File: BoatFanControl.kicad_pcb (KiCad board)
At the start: 2 copper layers, 34 x 34.8 mm, 11 parts, among them J1 Conn_01x04, Q1 IRLIZ44N, SW1 SW_Push, U1 Digispark

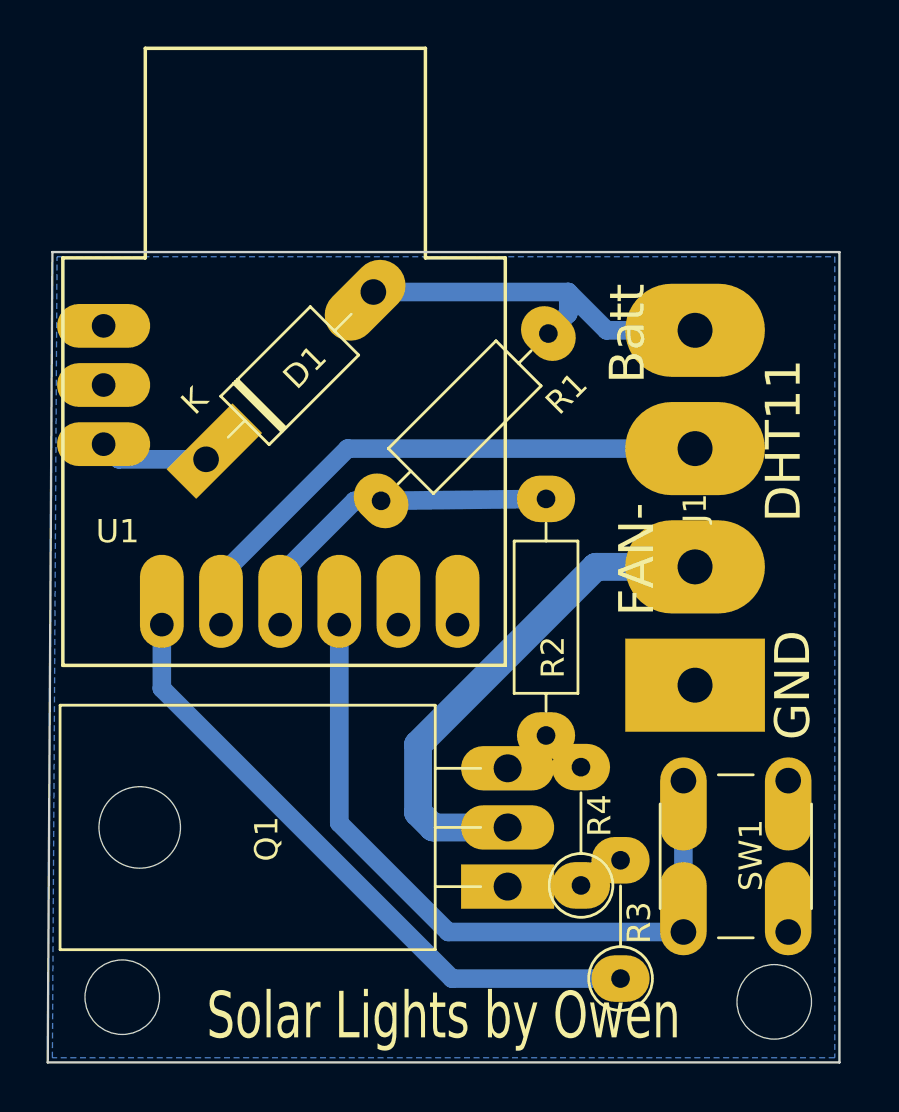
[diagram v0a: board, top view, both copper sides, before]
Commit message: Updated with seperate DHT11 mount
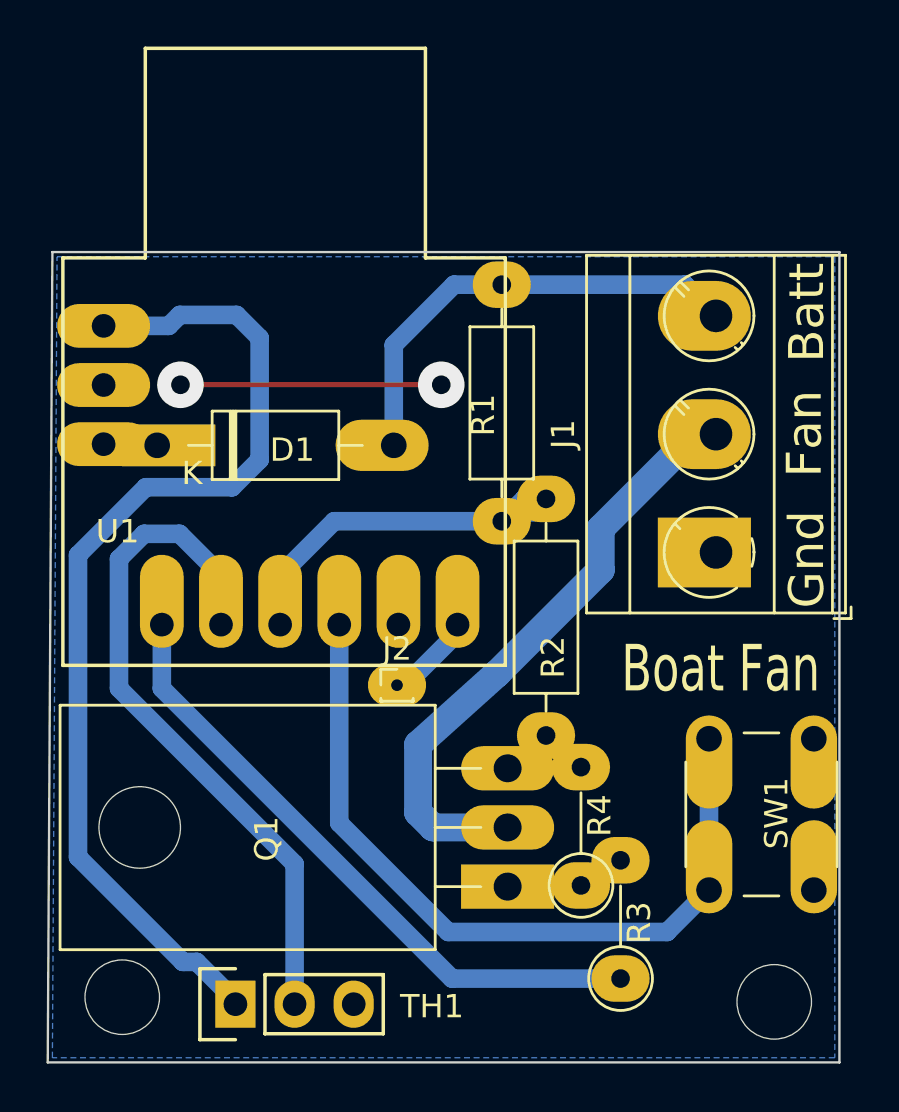
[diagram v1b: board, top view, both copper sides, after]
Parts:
- added J2: Reset, Connector_PinHeader_1.00mm:PinHeader_1x01_P1.00mm_Vertical, F.Cu at (100.0, 83.6)
- added TH1: DHT11, sensors:DHT11_Temperature_Humidity, F.Cu at (95.6, 97.3)
- J1: value Conn_01x04 -> Batt; footprint Connector_Wire:SolderWirePad_1x04_P5.08mm_Drill1.5mm -> TerminalBlock_MetzConnect:TerminalBlock_MetzConnect_Type073_RT02603HBLU_1x03_P5.08mm_Horizontal
- Q1: value IRLIZ44N -> IRLZ14
- R2: value 100R -> 1K
- moved J1 5.77 mm to (113.7, 77.9)
- moved R1 2.90 mm to (104.5, 66.4), turned to 270 degrees
- moved D1 2.18 mm to (89.7, 73.3), turned to 0 degrees
- moved SW1 2.11 mm to (117.9, 85.9)
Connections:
- J1 pad 3: DHT11 -> Vin
- U1 pad 6: (no net) -> Reset
- U1 pad 9: (no net) -> +5V
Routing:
- net +5V: track 0.00 -> 44.5 mm
- net GND: track 2.69 -> 13.9 mm, vias 0 -> 2
- net DHT11: track 24.7 -> 29.9 mm
- net FAN-gnd: track 22.1 -> 26.3 mm
- net Reset: track 0.00 -> 3.88 mm
- net Vin: track 16.6 -> 19.8 mm
- net +BATT: track 4.67 -> 2.32 mm
- net button: track 31.7 -> 33.6 mm
- net Vin-sense: track 14.9 -> 15.7 mm
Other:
- board text added: "Boat Fan"
- board text added: "Fan"
- board text added: "Gnd"
- board text removed: "DHT11"
- board text removed: "FAN-"
- board text removed: "GND"
- board text removed: "Solar Lights by Owen"

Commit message: Case, make PCB square..
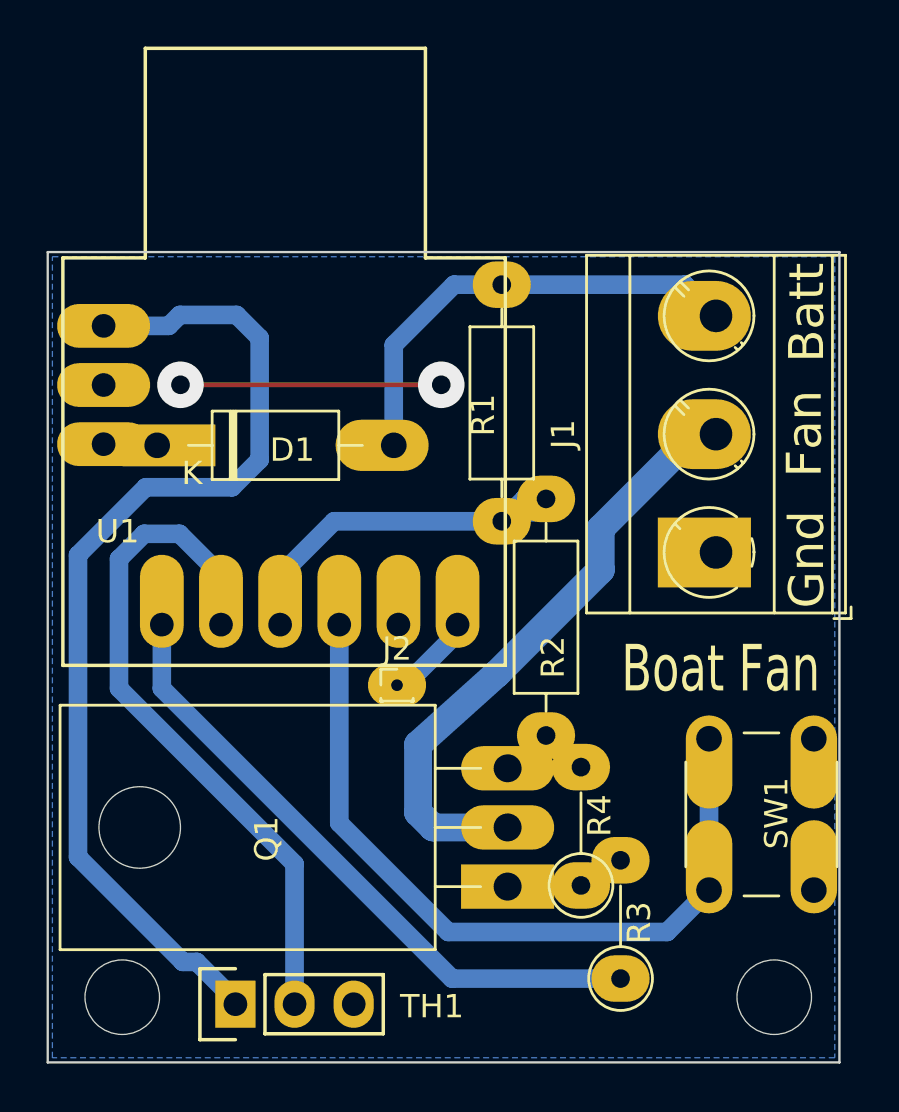
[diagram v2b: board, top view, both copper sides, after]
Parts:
- moved H2 0.20 mm to (116.2, 97.0)
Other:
- outline, holes or cut-outs redrawn
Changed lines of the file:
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@@
     (add_net LED)
     (add_net "Net-(Q1-Pad1)")
-    (add_net "Net-(U1-Pad5)")
     (add_net Reset)
     (add_net Vin)
@@
   )
   (module MountingHole:MountingHole_3.2mm_M3 (layer F.Cu)
-    (at 116.2 97.2)
+    (at 116.2 97)
     (descr "Mounting Hole 3.2mm, no annular, M3")
     (tags "mounting hole 3.2mm no annular m3")
@@
       (effects (font (size 1 1) (thickness 0.15)))
     )
+    (fp_text user %R (at 0.3 0) (layer F.Fab)
+      (effects (font (size 1 1) (thickness 0.15)))
+    )
+    (fp_circle (center 0 0) (end 3.2 0) (layer Cmts.User) (width 0.15))
     (fp_circle (center 0 0) (end 3.45 0) (layer F.CrtYd) (width 0.05))
-    (fp_circle (center 0 0) (end 3.2 0) (layer Cmts.User) (width 0.15))
-    (fp_text user %R (at 0.3 0) (layer F.Fab)
-      (effects (font (size 1 1) (thickness 0.15)))
-    )
     (pad 1 np_thru_hole circle (at 0 0) (size 3.2 3.2) (drill 3.2) (layers *.Cu *.Mask))
   )
@@
     (effects (font (size 2 1.4) (thickness 0.2)))
   )
-  (gr_line (start 85.2 65) (end 85 99.8) (layer Edge.Cuts) (width 0.1))
-  (gr_line (start 119 65) (end 85.2 65) (layer Edge.Cuts) (width 0.1))
+  (gr_line (start 85 65) (end 85 99.8) (layer Edge.Cuts) (width 0.1))
+  (gr_line (start 119 65) (end 85 65) (layer Edge.Cuts) (width 0.1))
   (gr_line (start 119 99.8) (end 119 65) (layer Edge.Cuts) (width 0.1))
   (gr_line (start 85 99.8) (end 119 99.8) (layer Edge.Cuts) (width 0.1))
@@
     (polygon
       (pts
-        (xy 85.4 65.2) (xy 118.8 65.2) (xy 118.8 99.6) (xy 85.2 99.6)
+        (xy 85.2 65.2) (xy 118.8 65.2) (xy 118.8 99.6) (xy 85.2 99.6)
       )
     )
